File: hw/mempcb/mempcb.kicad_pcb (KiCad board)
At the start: 4 copper layers, 100 x 100 mm, 31 parts, among them J1 RC6502_Bus, J2 0.1" 2x25, U3 JEDEC_DIP32_RAM, U4 74LS138, U5 74LS138

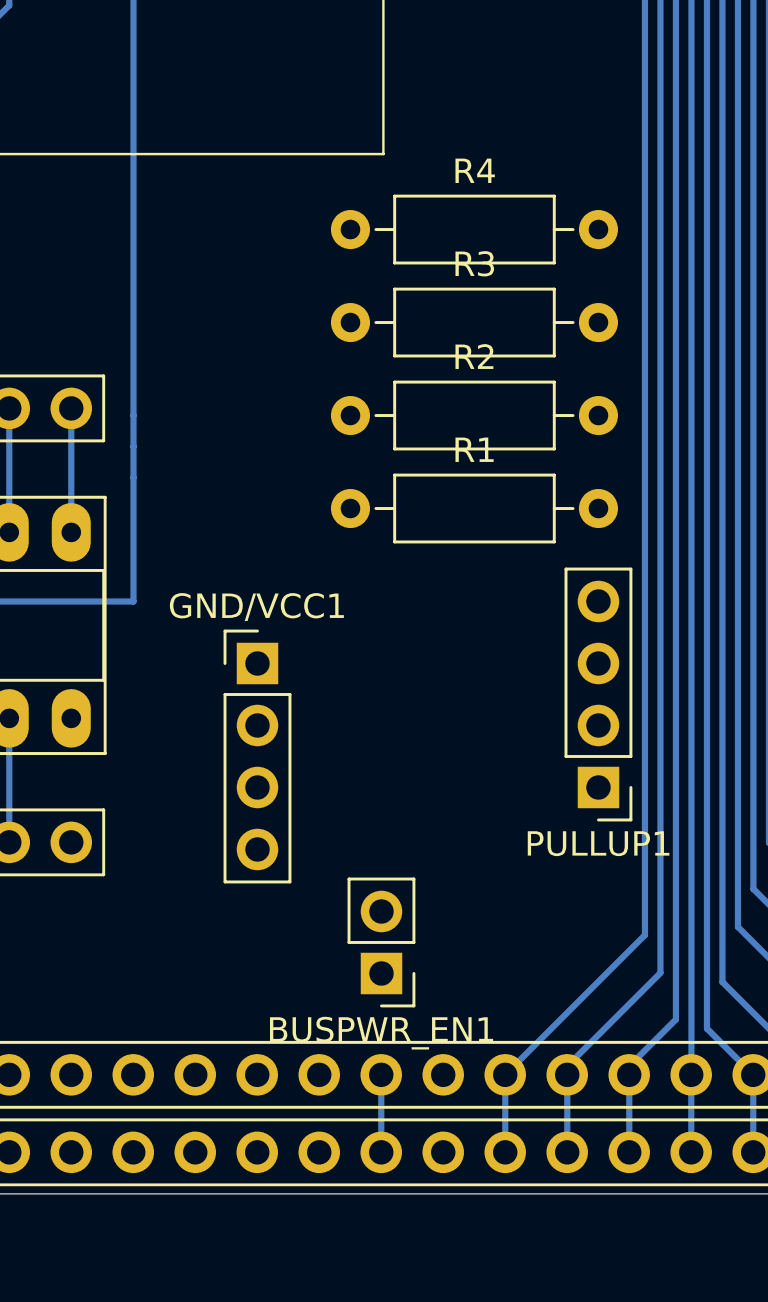
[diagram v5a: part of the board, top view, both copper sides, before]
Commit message: hw/mempcb: New GND/Vcc WW pins: 4×GND, 2×Vcc, side by side w/buspwr jumper
The BUS_VCC jumper is now directly above the RC6502 bus Vcc pins, and the
two wire-wrap Vcc pins are directly above that. Directly to its right,
above the RC6502 bus GND, we have four wire-wrap pins for GND. (These
latter have traces on the bottom just to make this easier to recognise when
looking at the backside; they still should be connected to the top ground
fill when we get to that.)

These and the pull-up wire-wrap headers are oriented vertically to make
routing of wire-wrap easier.

All of these, including the pull-ups, are now routed.
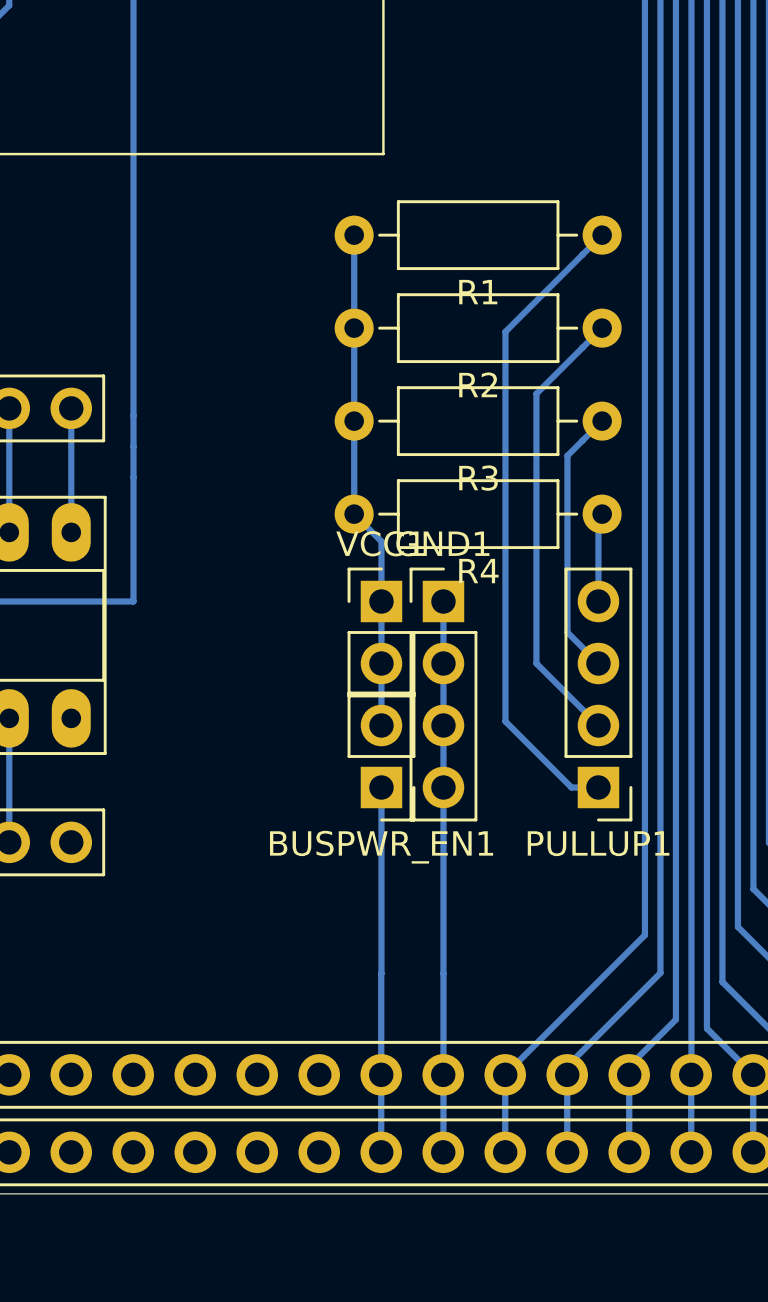
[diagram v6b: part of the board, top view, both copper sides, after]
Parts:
- removed GND/VCC1: 0.1" 1x4, Connector_PinHeader_2.54mm:PinHeader_1x04_P2.54mm_Vertical
- added GND1: 0.1" 1x4, Connector_PinHeader_2.54mm:PinHeader_1x04_P2.54mm_Vertical, F.Cu at (138.4, 125.7)
- added VCC1: 0.1" 1x2, Connector_PinHeader_2.54mm:PinHeader_1x02_P2.54mm_Vertical, F.Cu at (135.9, 125.7)
- moved R4 15.6 mm to (144.9, 122.1), turned to 180 degrees
- moved R1 15.2 mm to (144.9, 110.7), turned to 180 degrees
- moved R3 11.1 mm to (144.9, 118.3), turned to 180 degrees
- moved R2 10.9 mm to (144.9, 114.5), turned to 180 degrees
- moved BUSPWR_EN1 7.62 mm to (135.9, 133.3)
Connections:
- U3 pad 5: Net-(U3-Pad5) -> /A7
- W3_1 pad 5: Net-(U3-Pad5) -> /A7
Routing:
- net Net-(PULLUP1-Pad1): track 0.00 -> 26.5 mm
- net /GND: track 0.00 -> 22.6 mm
- net /VCC: track 162.9 -> 183.5 mm
- net Net-(PULLUP1-Pad2): track 0.00 -> 18.4 mm
- net /BUS_VCC: track 3.18 -> 15.0 mm
- net Net-(PULLUP1-Pad3): track 0.00 -> 11.0 mm
- net Net-(U3-Pad5): track 10.2 -> 0.00 mm
- net /A7: track 106.2 -> 116.4 mm
- net Net-(PULLUP1-Pad4): track 0.00 -> 3.64 mm

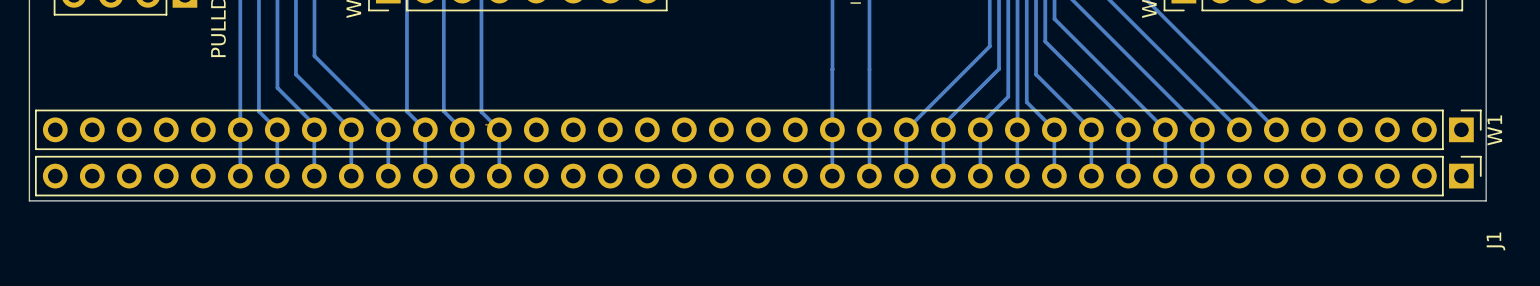
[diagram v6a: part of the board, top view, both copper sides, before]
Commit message: hw/mempcb: Finish routing RC6502 bus wire-wrap header
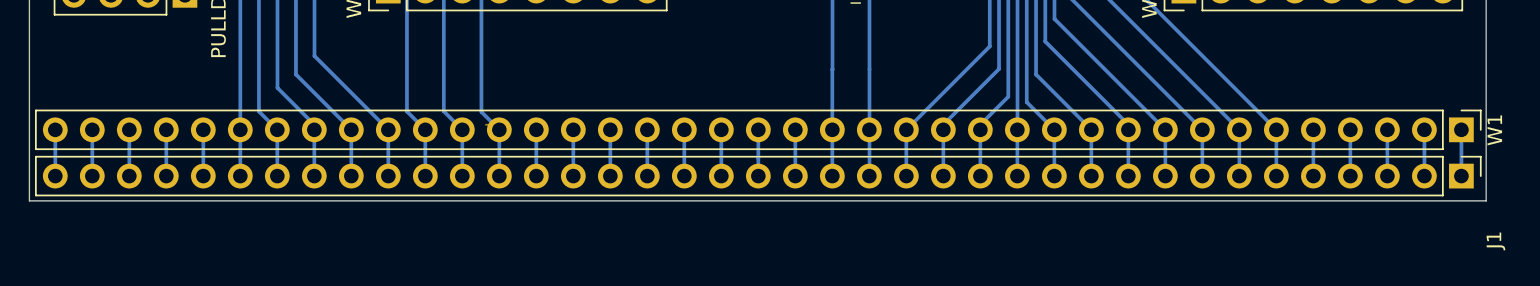
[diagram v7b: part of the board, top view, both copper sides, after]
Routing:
- net Net-(J1-Pad5): track 0.00 -> 3.18 mm
- net Net-(J1-Pad4): track 0.00 -> 3.18 mm
- net Net-(J1-Pad39): track 0.00 -> 3.18 mm
- net Net-(J1-Pad38): track 0.00 -> 3.18 mm
- net Net-(J1-Pad37): track 0.00 -> 3.18 mm
- net Net-(J1-Pad36): track 0.00 -> 3.18 mm
- net Net-(J1-Pad35): track 0.00 -> 3.18 mm
- net Net-(J1-Pad3): track 0.00 -> 3.18 mm
- net Net-(J1-Pad26): track 0.00 -> 3.18 mm
- net Net-(J1-Pad25): track 0.00 -> 3.18 mm
- net Net-(J1-Pad24): track 0.00 -> 3.18 mm
- net Net-(J1-Pad23): track 0.00 -> 3.18 mm
- net Net-(J1-Pad22): track 0.00 -> 3.18 mm
- net Net-(J1-Pad21): track 0.00 -> 3.18 mm
- net Net-(J1-Pad20): track 0.00 -> 3.18 mm
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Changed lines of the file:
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@@
     (thickness 1.6002)
     (drawings 4)
-    (tracks 514)
+    (tracks 535)
     (zones 0)
     (modules 32)
@@
   (segment (start 135.89 140.97) (end 135.89 133.35) (width 0.254) (layer Back) (net 2))
   (segment (start 135.88 140.98) (end 135.89 140.97) (width 0.254) (layer Back) (net 2))
+  (segment (start 82.54 145.123) (end 82.54 148.298) (width 0.254) (layer Back) (net 3))
+  (segment (start 85.08 148.298) (end 85.08 145.123) (width 0.254) (layer Back) (net 4))
+  (segment (start 87.62 145.123) (end 87.62 148.298) (width 0.254) (layer Back) (net 5))
+  (segment (start 90.16 145.123) (end 90.16 148.298) (width 0.254) (layer Back) (net 6))
+  (segment (start 92.7 148.298) (end 92.7 145.123) (width 0.254) (layer Back) (net 7))
   (segment (start 132.07 87.338) (end 144.77 87.338) (width 0.254) (layer Back) (net 8))
   (segment (start 95.24 148.298) (end 95.24 145.123) (width 0.254) (layer Back) (net 8))
@@
   (segment (start 120.64 101.308) (end 111.788999 110.159001) (width 0.254) (layer Back) (net 15))
   (segment (start 120.64 91.148) (end 120.64 101.308) (width 0.254) (layer Back) (net 15))
+  (segment (start 115.56 148.298) (end 115.56 145.123) (width 0.254) (layer Back) (net 16))
+  (segment (start 118.1 145.123) (end 118.1 148.298) (width 0.254) (layer Back) (net 17))
+  (segment (start 120.64 148.298) (end 120.64 145.123) (width 0.254) (layer Back) (net 18))
+  (segment (start 123.18 145.123) (end 123.18 148.298) (width 0.254) (layer Back) (net 19))
+  (segment (start 125.72 148.298) (end 125.72 145.123) (width 0.254) (layer Back) (net 20))
+  (segment (start 128.26 145.123) (end 128.26 148.298) (width 0.254) (layer Back) (net 21))
+  (segment (start 130.8 147.095919) (end 130.8 145.123) (width 0.254) (layer Back) (net 22))
+  (segment (start 130.8 148.298) (end 130.8 147.095919) (width 0.254) (layer Back) (net 22))
+  (segment (start 133.34 145.123) (end 133.34 148.298) (width 0.254) (layer Back) (net 23))
   (segment (start 138.43 133.35) (end 138.43 125.73) (width 0.254) (layer Back) (net 24))
   (segment (start 138.43 148.288) (end 138.42 148.298) (width 0.254) (layer Back) (net 24))
@@
   (segment (start 144.77 84.798) (end 132.07 84.798) (width 0.254) (layer Back) (net 105))
   (segment (start 106.67 69.558) (end 116.83 69.558) (width 0.254) (layer Back) (net 32))
+  (segment (start 163.82 148.298) (end 163.82 145.123) (width 0.254) (layer Back) (net 34))
+  (segment (start 166.36 145.123) (end 166.36 148.298) (width 0.254) (layer Back) (net 35))
+  (segment (start 168.9 148.298) (end 168.9 145.123) (width 0.254) (layer Back) (net 36))
+  (segment (start 171.44 145.123) (end 171.44 148.298) (width 0.254) (layer Back) (net 37))
+  (segment (start 173.98 148.298) (end 173.98 145.123) (width 0.254) (layer Back) (net 38))
+  (segment (start 176.52 145.123) (end 176.52 148.298) (width 0.254) (layer Back) (net 39))
+  (segment (start 179.06 148.298) (end 179.06 145.123) (width 0.254) (layer Back) (net 40))
   (segment (start 144.78 122.300699) (end 144.931268 122.149431) (width 0.254) (layer Back) (net 95))
   (segment (start 144.78 125.73) (end 144.78 122.300699) (width 0.254) (layer Back) (net 95))

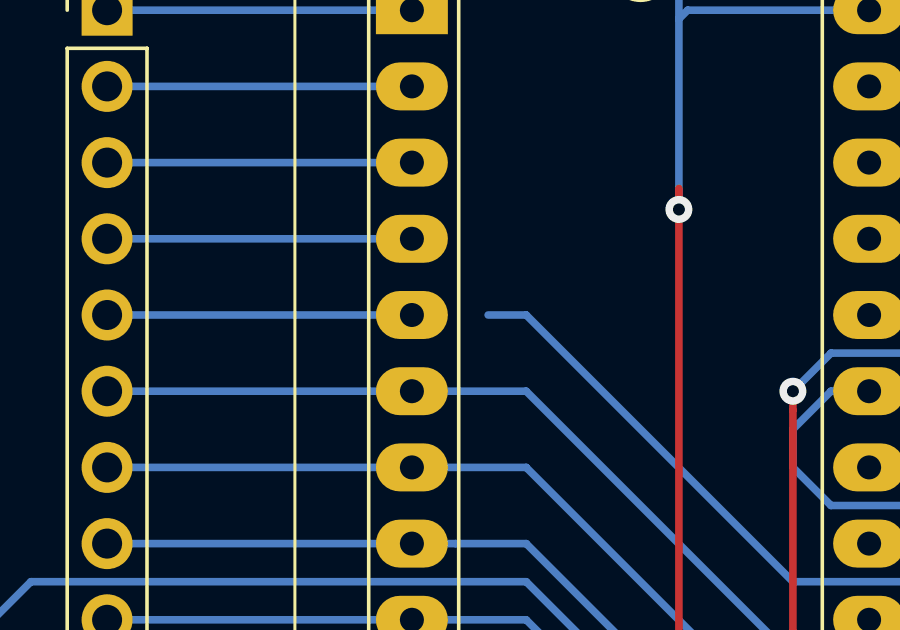
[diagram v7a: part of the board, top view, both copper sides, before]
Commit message: hw/mempcb: Hook up A7, now that it's appeared on the DIP-32
I don't know why this appeared now, but not before for me.
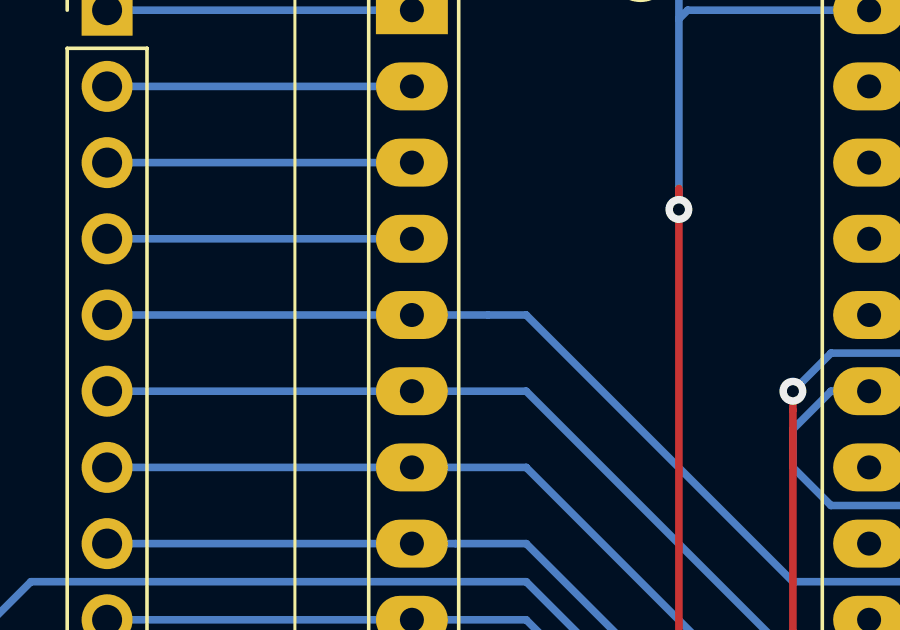
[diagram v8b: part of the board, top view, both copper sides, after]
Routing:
- net /A7: track 116.4 -> 118.9 mm
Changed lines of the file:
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@@
     (thickness 1.6002)
     (drawings 4)
-    (tracks 535)
+    (tracks 536)
     (zones 0)
     (modules 32)
@@
   (segment (start 144.77 84.798) (end 132.07 84.798) (width 0.254) (layer Back) (net 105))
   (segment (start 106.67 69.558) (end 116.83 69.558) (width 0.254) (layer Back) (net 32))
+  (segment (start 119.37 69.558) (end 116.83 69.558) (width 0.254) (layer Back) (net 32))
   (segment (start 163.82 148.298) (end 163.82 145.123) (width 0.254) (layer Back) (net 34))
   (segment (start 166.36 145.123) (end 166.36 148.298) (width 0.254) (layer Back) (net 35))
